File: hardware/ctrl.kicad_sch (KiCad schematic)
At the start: 24 parts, among them J1 USB_C_Receptacle_USB2.0_16P, SW2 SW_Push, U1 ESP32-C3-WROOM-02

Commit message: general schematic and PCB clean
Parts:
- J1: LCSC C2894897 -> C393939
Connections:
- net WIFI_~{ENABLE}: no longer names the net of U1.4 (IO5)
- no-connect marks 4 -> 5
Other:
- note removed: "Difficult to place! Missing 3D model"
- moved on the sheet: C25, C3, D5, J1, LED1, R1, R2, R3, R40, TH1

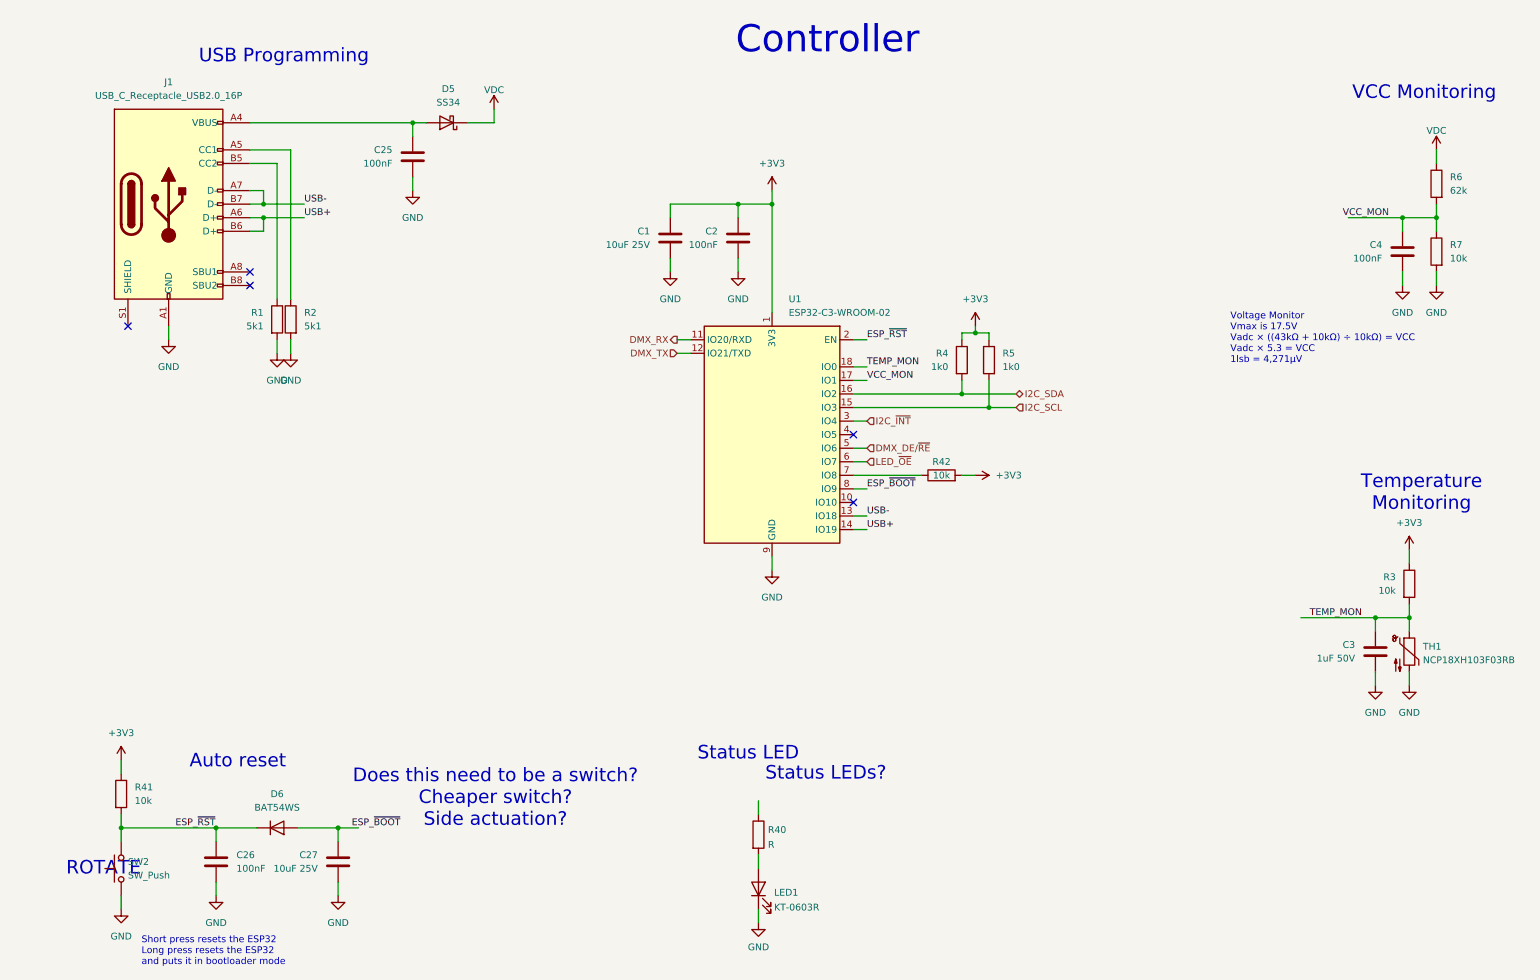
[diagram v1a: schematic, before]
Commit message: sorting button and LED
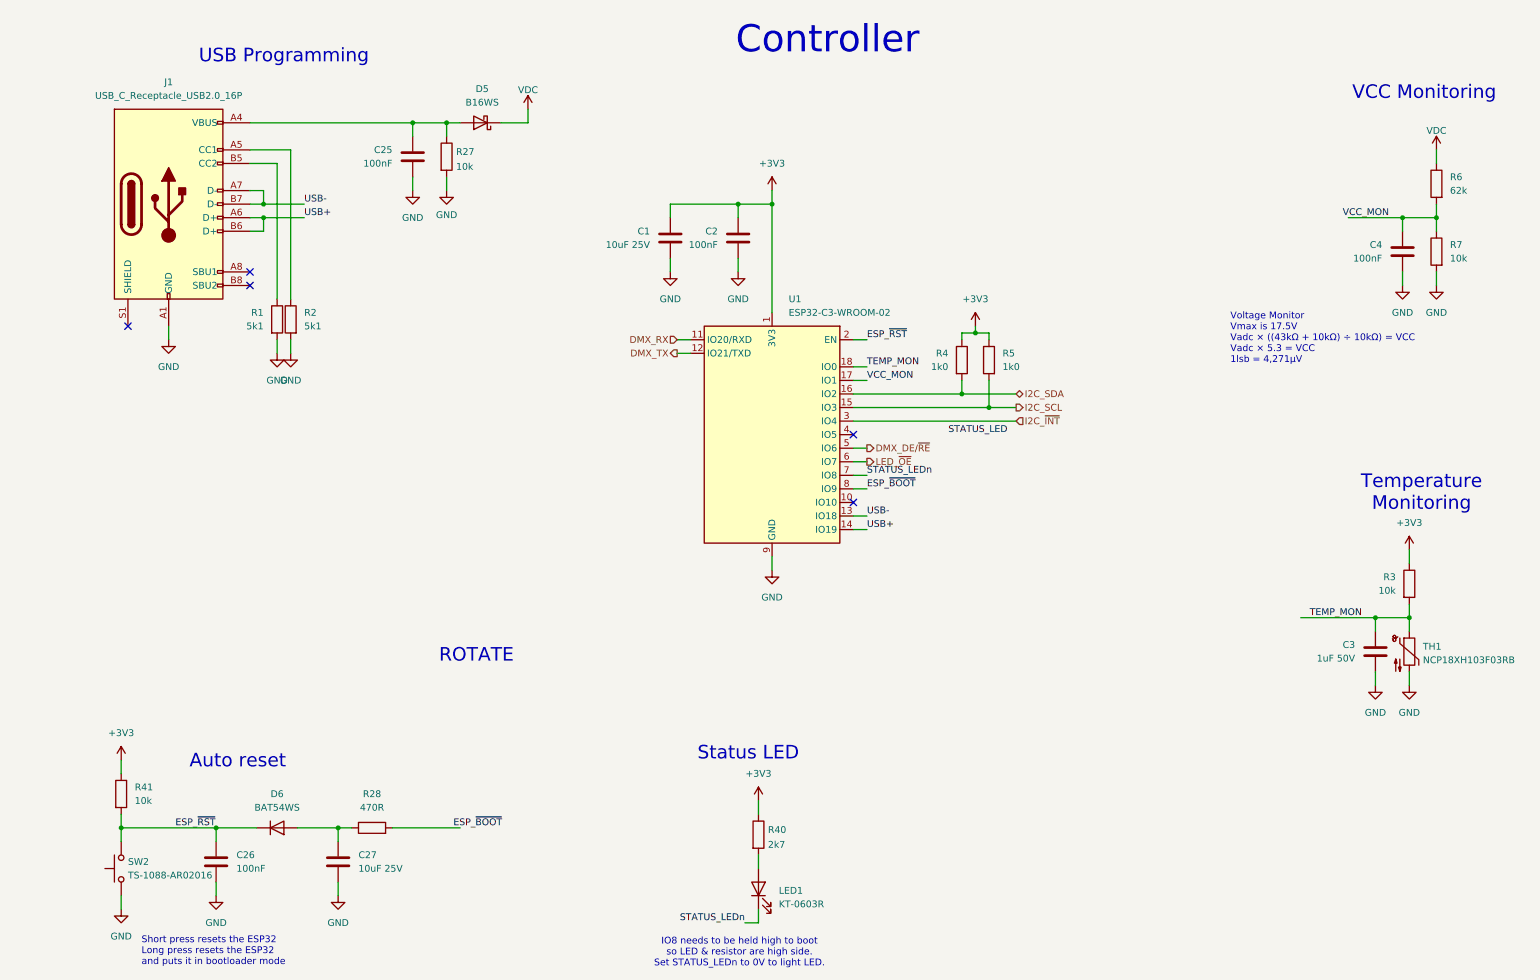
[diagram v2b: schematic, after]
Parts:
- removed R42: 10k, Resistor_SMD:R_0603_1608Metric, symbol Device:R
- added R27: 10k, Resistor_SMD:R_0603_1608Metric, symbol Device:R
- added R28: 470R, Resistor_SMD:R_0603_1608Metric, symbol Device:R
- D5: value SS34 -> B16WS; footprint Diode_SMD:D_SMA -> Diode_SMD:D_SOD-323; LCSC C8678 -> C7420327; Rotation Offset (none) -> 180
- R40: value R -> 2k7; LCSC (none) -> C13167
- SW2: value SW_Push -> TS-1088-AR02016; footprint Button_Switch_SMD:SW_SPST_B3U-1000P -> Button_Switch_SMD:SW_Push_SPST_NO_Alps_SKRK; LCSC C231329 -> C720477
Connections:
- net +3V3: now also R40.1
- net ESP_~{BOOT}: now also R28.2; no longer C27.1, D6.2 (A)
- net GND: now also R27.2; no longer LED1.1 (K)
- net at C25.1, D5.2 (A), J1.A4 (VBUS)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: now also R27.1
- net STATUS_LEDn: now reaches U1.7 (IO8)
- net STATUS_LEDn: now also LED1.1 (K)
- new net: C27.1, D6.2 (A), R28.1
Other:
- note added: "IO8 needs to be held high to boot so LED & resistor are high side. Set STATUS_LEDn to 0V to light LED."
- note removed: "Does this need to be a switch? Cheaper switch? Side actuation?"
- note removed: "Status LEDs?"
- moved on the sheet: D5

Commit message: starting layout
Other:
- note removed: "ROTATE"
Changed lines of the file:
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@@
 		(company "Wires & Bits")
-	)
-	(text "ROTATE"
-		(exclude_from_sim no)
-		(at 88.138 134.112 0)
-		(effects
-			(font
-				(size 2.54 2.54)
-				(color 255 0 0 1)
-			)
-		)
 	)
 	(text "Auto reset"
@@
 		(effects
 			(font
+				(size 1.27 1.27)
+			)
+			(justify left)
+		)
+	)
+	(hierarchical_label "LED_~{PGD}"
+		(shape input)
+		(at 180.34 102.87 0)
+		(effects
+			(font

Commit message: more layout and fixing OOS items
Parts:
- C1, C2, C25, C26, C27, C3, C4: symbol Device:C -> emf_beacon_ibrary:C
- D5: symbol Device:D_Schottky -> emf_beacon_ibrary:D_Schottky
- D6: symbol Device:D -> emf_beacon_ibrary:D
- J1: symbol Connector:USB_C_Receptacle_USB2.0_16P -> emf_beacon_ibrary:USB_C_Receptacle_USB2.0_16P
- LED1: symbol Device:LED -> emf_beacon_ibrary:LED
- R1, R2, R27, R28, R3, R4, R40, R41, R5, R6, R7: symbol Device:R -> emf_beacon_ibrary:R
- SW2: symbol Switch:SW_Push -> emf_beacon_ibrary:SW_Push
- TH1: symbol Device:Thermistor_NTC -> emf_beacon_ibrary:Thermistor_NTC
- U1: symbol RF_Module:ESP32-C3-WROOM-02 -> emf_beacon_ibrary:ESP32-C3-WROOM-02

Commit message: preparing for release
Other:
- title: (none) -> Controller
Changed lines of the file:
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@@
 	(paper "A4")
 	(title_block
-		(date "2026-04-10")
-		(rev "0")
+		(title "Controller")
+		(date "2026-06-05")
+		(rev "1")
 		(company "Wires & Bits")
 	)
